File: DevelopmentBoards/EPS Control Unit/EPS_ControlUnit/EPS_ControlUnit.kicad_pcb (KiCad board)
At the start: 2 copper layers, 55.1 x 45.2 mm, 51 parts, among them U1 STM32L476VET6, U2 AMS1117-3.3, U3 TPS3824-33QDBVRQ1, Y1 32MHz

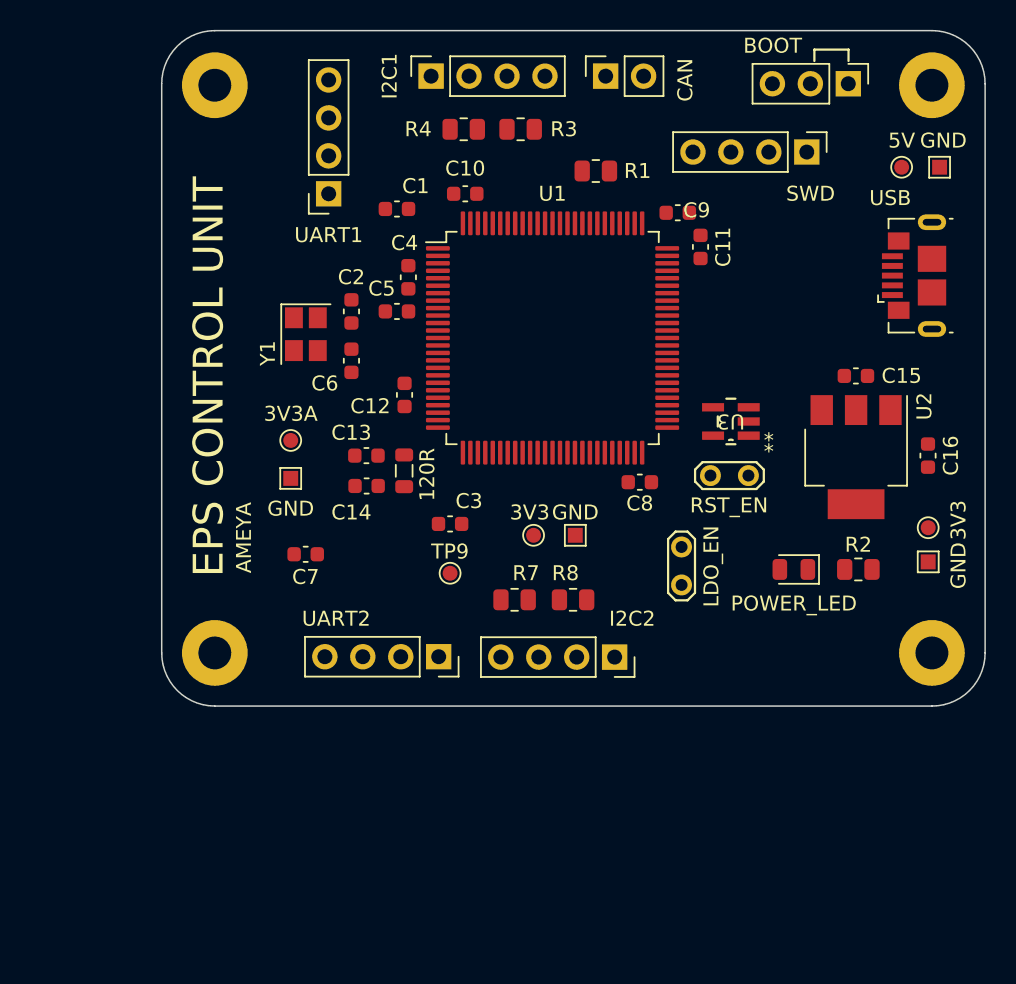
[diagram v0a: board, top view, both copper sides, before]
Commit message: EPS Control Unit Dev Board Completed
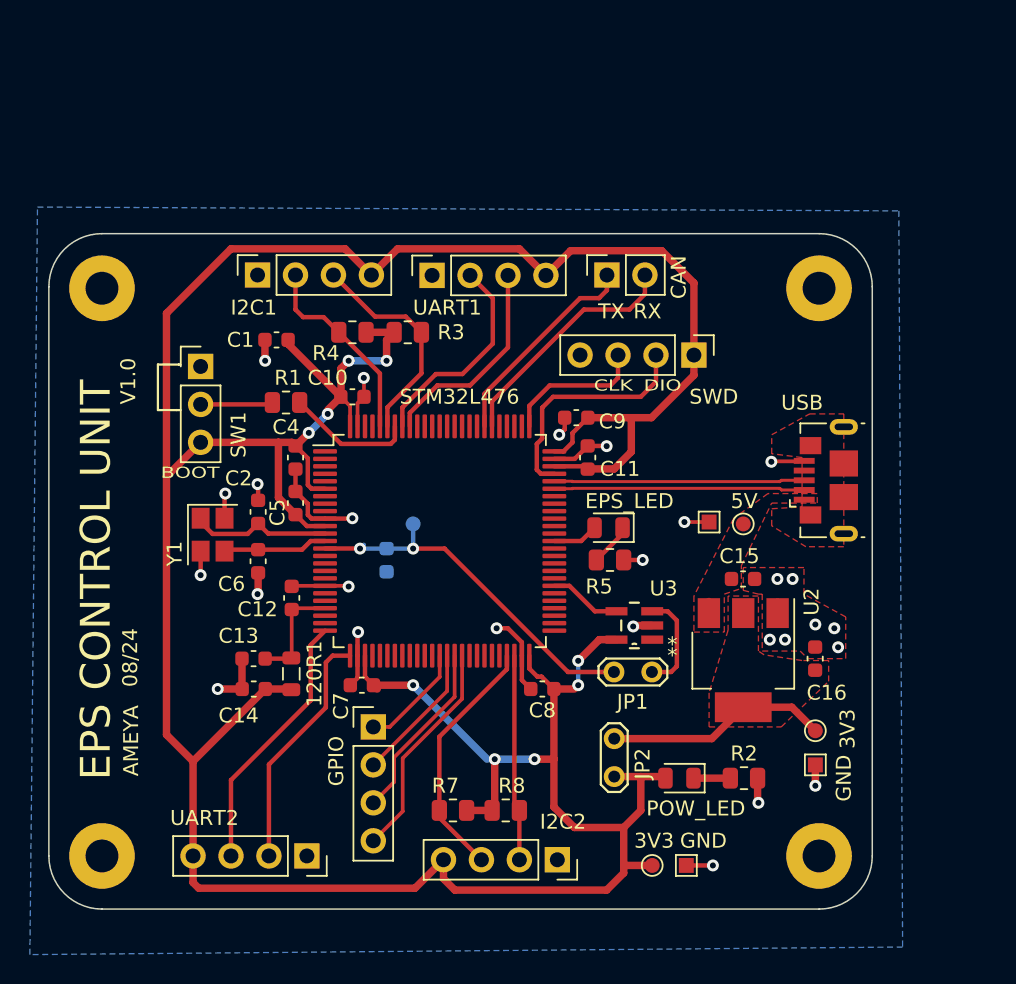
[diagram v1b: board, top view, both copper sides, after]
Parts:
- removed 3V3A: TestPoint, TestPoint:TestPoint_Pad_D1.0mm
- removed the GND at (129.0, 86.4)
- added EPS_LED: EPS_LED, LED_SMD:LED_0805_2012Metric, F.Cu at (150.3, 89.7)
- added G***: LOGO, LOGO, B.Cu at (126.0, 101.2)
- added J8: Conn_01x04_Pin, Connector_PinHeader_2.54mm:PinHeader_1x04_P2.54mm_Vertical, F.Cu at (134.6, 103.0)
- added R5: 1k5, Resistor_SMD:R_0805_2012Metric, F.Cu at (150.4, 91.8)
- C3: moved to B.Cu
- NRST: renamed from TP9; moved to B.Cu
- POW_LED: renamed from POWER_LED; value EPS_LED -> POWER_LED
- moved SW1 47.3 mm to (123.0, 78.9), turned to 0 degrees
- moved TP2 28.3 mm to (157.0, 89.3), turned to 180 degrees
- moved 5V 26.1 mm to (159.3, 89.4), turned to 180 degrees
- moved R1 25.9 mm to (128.7, 81.3), turned to 0 degrees
- moved 3V3 23.5 mm to (153.2, 112.3)
- moved GND 23.3 mm to (155.5, 112.3)
- moved J3 17.7 mm to (126.8, 72.7)
- moved C11 16.0 mm to (148.9, 85.0)
- moved UART2 16.0 mm to (130.1, 111.6)
- moved POW_LED 15.9 mm to (155.1, 106.4)
- moved R2 15.9 mm to (159.4, 106.4)
- moved C10 15.5 mm to (133.2, 80.9)
- moved C15 15.5 mm to (159.3, 93.1)
- moved C16 15.5 mm to (164.1, 98.4)
- moved GND 15.5 mm to (164.2, 105.5)
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- renumbered 120R to 120R1, SWD to J1, I2C1 to J3, UART1 to J4, I2C2 to J5, CAN to J7, RST_EN to JP1, LDO_EN to JP2, U1 to STM32L476, BOOT to SW1, GND to TP2
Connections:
- H1 pad 1: unconnected-(H1-Pad1) -> GND
- H2 pad 1: unconnected-(H2-Pad1) -> GND
- H3 pad 1: unconnected-(H3-Pad1) -> GND
- H4 pad 1: unconnected-(H4-Pad1) -> GND
- STM32L476 pad 38: unconnected-(U1-PE7-Pad38) -> /GPIO1
- STM32L476 pad 39: unconnected-(U1-PE8-Pad39) -> /GPIO2
- STM32L476 pad 40: unconnected-(U1-PE9-Pad40) -> /GPIO3
- STM32L476 pad 41: unconnected-(U1-PE10-Pad41) -> /GPIO4
- STM32L476 pad 63: unconnected-(U1-PC6-Pad63) -> /EPS_LED
- USB pad 6: unconnected-(J2-Shield-Pad6) -> GND
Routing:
- net 3V3_EPS: track 0.00 -> 245.8 mm, vias 0 -> 9
- net GND: track 0.00 -> 51.8 mm, vias 0 -> 27
- net /NRST: track 0.00 -> 24.6 mm, vias 0 -> 2
- net /UART2_TX: track 0.00 -> 17.7 mm
- net /I2C2_SCL: track 0.00 -> 16.8 mm
- net /UART2_RX: track 0.00 -> 16.3 mm
- net /USB_D-: track 0.00 -> 16.3 mm
- net /USB_D+: track 0.00 -> 16.3 mm
- net /CAN_RX: track 0.00 -> 16.2 mm
- net /SWDIO: track 0.00 -> 15.7 mm
- net /3V3_LDO: track 0.00 -> 15.0 mm
- net /GPIO4: track 0.00 -> 14.9 mm
- net /I2C1_SCL: track 0.00 -> 14.7 mm
- net /UART1_RX: track 0.00 -> 14.3 mm
- net /CAN_TX: track 0.00 -> 14.3 mm
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- added copper zone on F.Cu, net /3V3_LDO
- added copper zone on B.Cu, net GND
- added copper zone on F.Cu, net GND
- added copper zone on F.Cu, net VBUS
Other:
- board text added: "08/24"
- board text added: "3V3"
- board text added: "ASSEMBLE WITH CARE -ORDER"
- board text added: "BOOT"
- board text added: "CAN"
- board text added: "CLK"
- board text added: "DIO"
- board text added: "GND"
- board text added: "GPIO"
- board text added: "I2C1"
- board text added: "I2C2"
- board text added: "MADE IN SATLAB"
- board text added: "RX"
- board text added: "SCL"
- board text added: "SDA"
- board text added: "SWD"
- board text added: "TX"
- board text added: "UART1"
- board text added: "V1.0"

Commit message: Final changes to EPS Control unit dev board
Added pinouts for ADC and DAC
Sent EPS Control unit for manufacturing
Started designing EPS PDB Board (Control Unit + Power Distribution and Regulation)
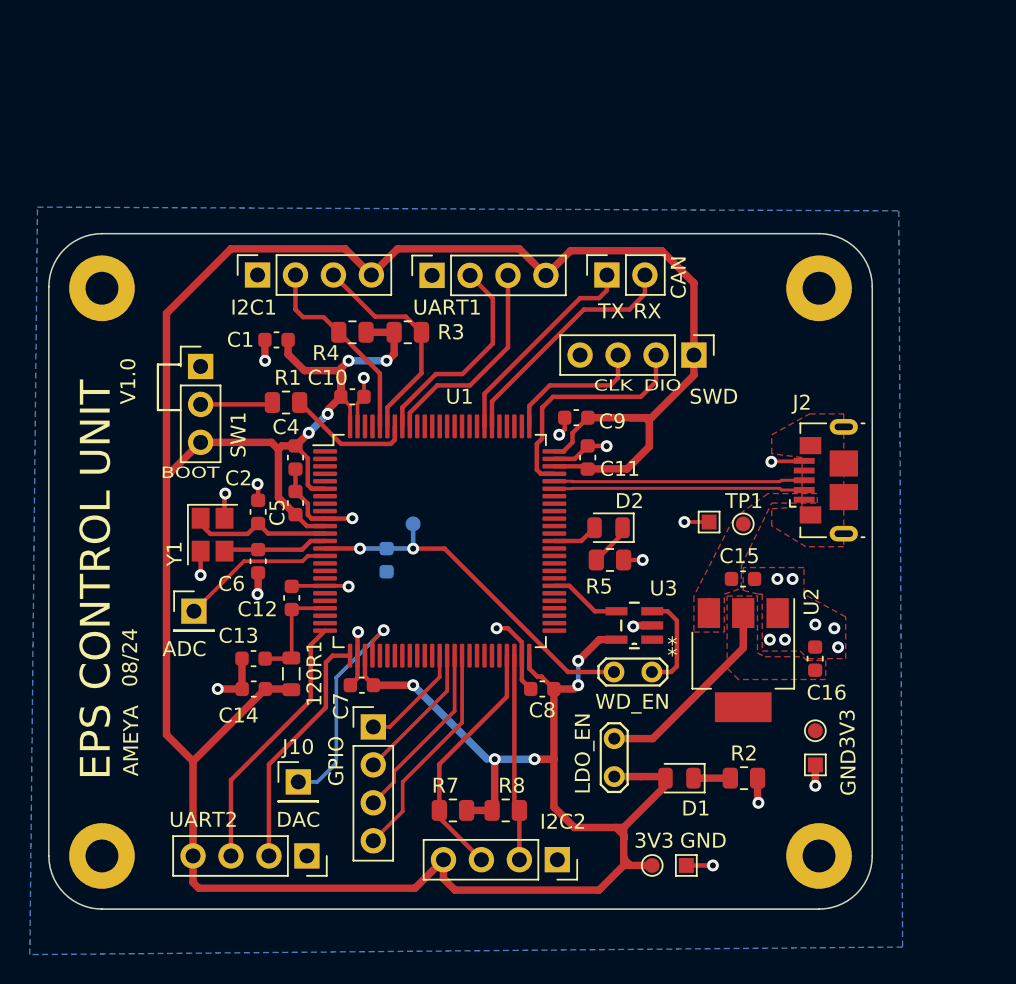
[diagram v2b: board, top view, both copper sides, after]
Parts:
- added J10: Conn_01x01_Pin, Connector_PinHeader_2.54mm:PinHeader_1x01_P2.54mm_Vertical, F.Cu at (129.5, 106.7)
- added J9: Conn_01x01_Pin, Connector_PinHeader_2.54mm:PinHeader_1x01_P2.54mm_Vertical, F.Cu at (122.6, 95.2)
- renumbered POW_LED to D1, EPS_LED to D2, USB to J2, UART2 to J6, JP2 to LDO_EN, 5V to TP1, NRST to TP9, STM32L476 to U1, JP1 to WD_EN
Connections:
- U1 pad 15: unconnected-(U1-PC0-Pad15) -> /ADC
- U1 pad 29: unconnected-(U1-PA4-Pad29) -> /DAC
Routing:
- net /DAC: track 0.00 -> 15.3 mm, vias 0 -> 1
- net /ADC: track 0.00 -> 10.3 mm
- net 3V3_EPS: track 245.8 -> 250.9 mm
- net /3V3_LDO: track 15.0 -> 13.5 mm
- net /SW_BOOT0: track 5.57 -> 4.86 mm
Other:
- board text added: "ADC"
- board text added: "DAC"
- board text added: "UART2"
